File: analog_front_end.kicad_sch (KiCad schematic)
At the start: 14 parts, among them J3 Conn_01x03_Pin, J4 Conn_01x03_Pin, Q3 BC847,215, Q4 BSS316N, U7 OPA388IDBV

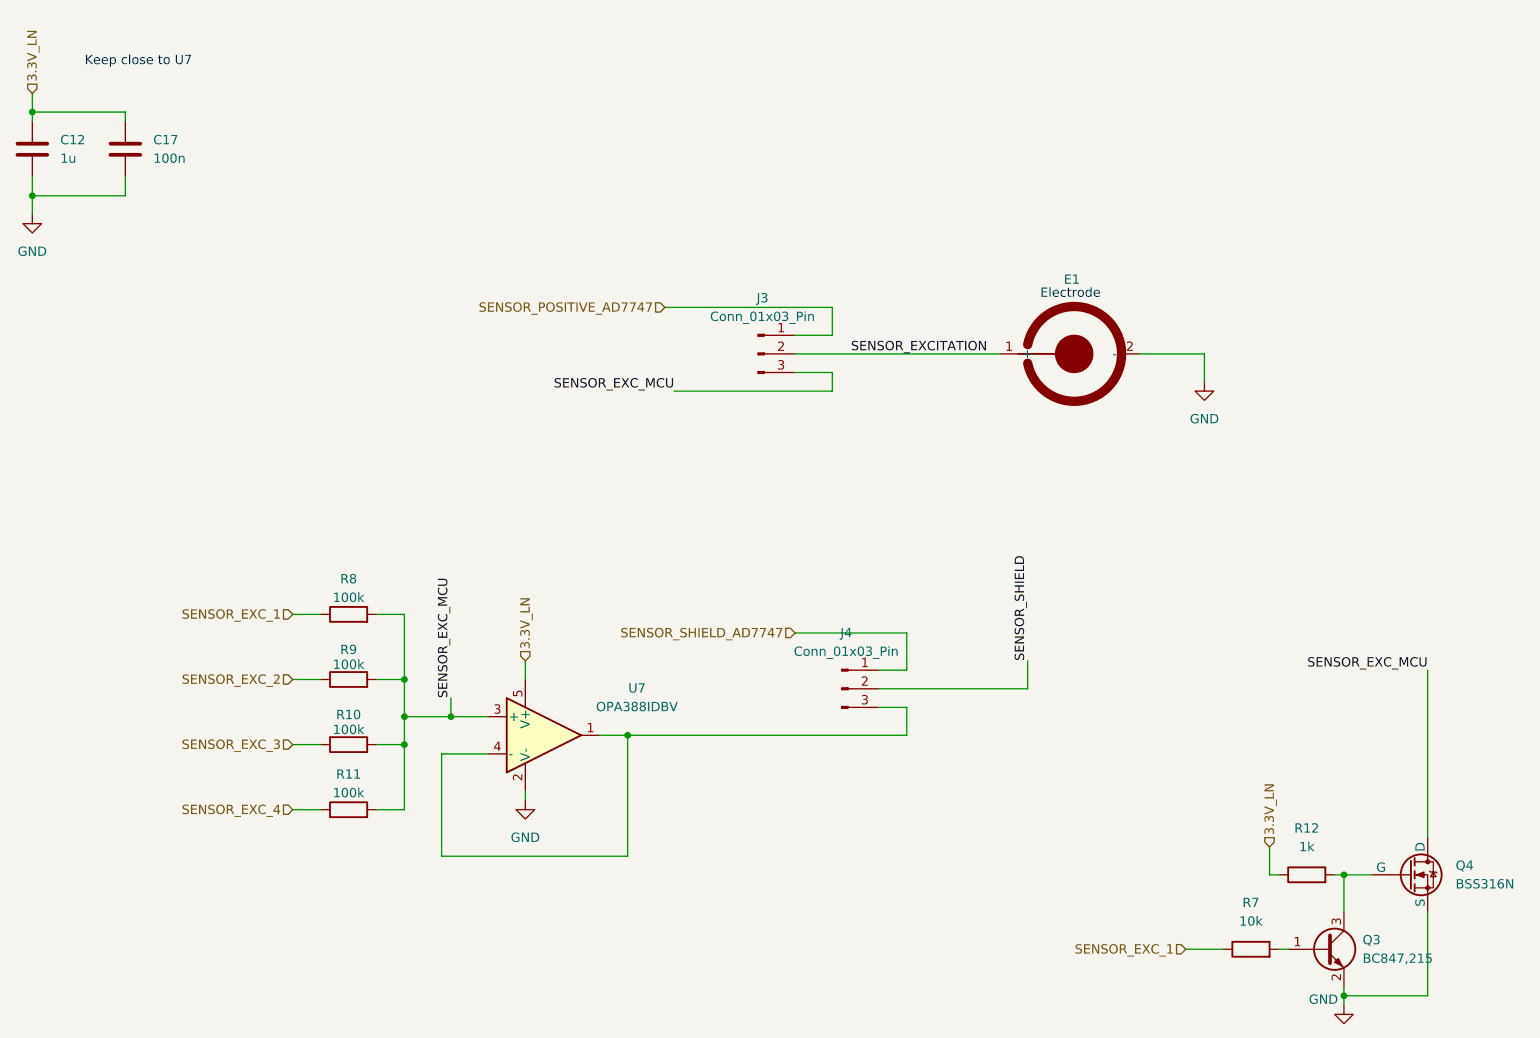
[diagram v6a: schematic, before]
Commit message: design: Assign LSCS and MPN reference to components
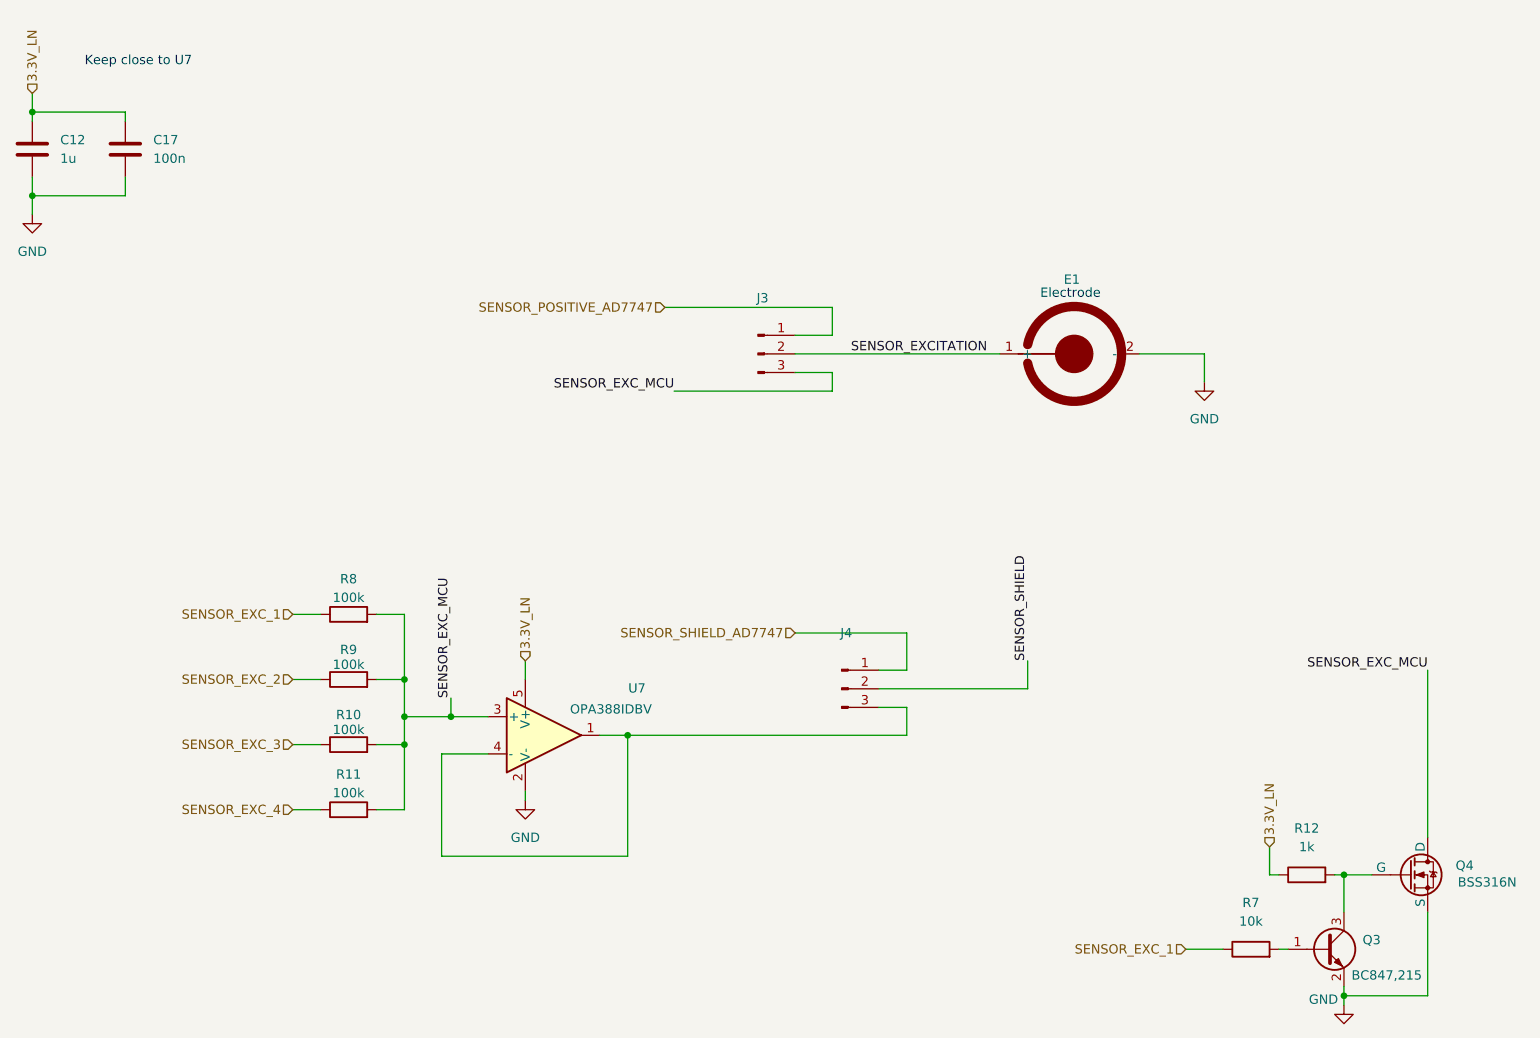
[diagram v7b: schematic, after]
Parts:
- C12: LCSC (none) -> C59782
- C17: LCSC (none) -> C14663
- E1: now left out of the parts list
- J3, J4: value Conn_01x03_Pin -> ~; LCSC (none) -> C5383112
- Q3: value BC847,215 -> ~; LCSC (none) -> C130417; MPN (none) -> BC847,215
- Q4: value BSS316N -> ~; LCSC (none) -> C19829413; MPN (none) -> BSS316N
- R10, R11, R8, R9: LCSC (none) -> C14675
- R12: LCSC (none) -> C22548
- R7: LCSC (none) -> C98220
- U7: value OPA388IDBV -> ~; LCSC (none) -> C1850240; MPN (none) -> OPA388IDBV
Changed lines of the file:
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@@
 		(on_board yes)
 		(dnp no)
-		(fields_autoplaced yes)
 		(property "Reference" "U7"
 			(at 99.06 105.3398 0)
@@
 			)
 		)
-		(property "Value" "OPA388IDBV"
+		(property "Value" "~"
 			(at 99.06 107.8798 0)
 			(effects
@@
 		)
 		(property "Description" "Operational amplifier, single"
+			(at 86.36 111.76 0)
+			(effects
+				(font
+					(size 1.27 1.27)
+				)
+				(hide yes)
+			)
+		)
+		(property "MPN" "OPA388IDBV"
+			(at 95.504 108.204 0)
+			(effects
+				(font
+					(size 1.27 1.27)
+				)
+			)
+		)
+		(property "LCSC" "C1850240"
 			(at 86.36 111.76 0)
 			(effects
@@
 			)
 		)
+		(property "LCSC" "C98220"
+			(at 182.88 140.97 0)
+			(effects
+				(font
+					(size 1.27 1.27)
+				)
+				(hide yes)
+			)
+		)
 		(pin "2"
 		)
@@
 			)
 		)
+		(property "LCSC" "C14675"
+			(at 59.69 113.03 0)
+			(effects
+				(font
+					(size 1.27 1.27)
+				)
+				(hide yes)
+			)
+		)
 		(pin "2"
 		)
@@
 		)
 		(property "Description" "Resistor"
+			(at 59.69 104.14 0)
+			(effects
+				(font
+					(size 1.27 1.27)
+				)
+				(hide yes)
+			)
+		)
+		(property "LCSC" "C14675"
 			(at 59.69 104.14 0)
 			(effects
@@
 			)
 		)
+		(property "LCSC" "C22548"
+			(at 190.5 130.81 0)
+			(effects
+				(font
+					(size 1.27 1.27)
+				)
+				(hide yes)
+			)
+		)
 		(pin "2"
 		)
@@
 		(on_board yes)
 		(dnp no)
-		(fields_autoplaced yes)
 		(property "Reference" "Q4"
 			(at 210.82 129.5399 0)
@@
 			)
 		)
-		(property "Value" "BSS316N"
+		(property "Value" "~"
 			(at 210.82 132.0799 0)
 			(effects
@@
 			)
 		)
-		(property "LCSC" ""
+		(property "LCSC" "C19829413"
 			(at 204.47 130.81 0)
 			(effects
@@
 				)
 				(hide yes)
+			)
+		)
+		(property "MPN" "BSS316N"
+			(at 215.138 131.826 0)
+			(effects
+				(font
+					(size 1.27 1.27)
+				)
 			)
 		)
@@
 			)
 		)
-		(property "Value" "Conn_01x03_Pin"
+		(property "Value" "~"
 			(at 116.205 54.61 0)
 			(effects
@@
 			)
 		)
+		(property "LCSC" "C5383112"
+			(at 115.57 59.69 0)
+			(effects
+				(font
+					(size 1.27 1.27)
+				)
+				(hide yes)
+			)
+		)
+		(property "MPN" ""
+			(at 115.57 59.69 0)
+			(effects
+				(font
+					(size 1.27 1.27)
+				)
+			)
+		)
 		(pin "3"
 		)
@@
 		(on_board yes)
 		(dnp no)
-		(fields_autoplaced yes)
 		(property "Reference" "Q3"
 			(at 198.12 139.6999 0)
@@
 			)
 		)
-		(property "Value" "BC847,215"
+		(property "Value" "~"
 			(at 198.12 142.2399 0)
 			(effects
@@
 			)
 		)
-		(property "LCSC" ""
+		(property "LCSC" "C130417"
 			(at 193.04 140.97 0)
 			(effects
@@
 				)
 				(hide yes)
+			)
+		)
+		(property "MPN" "BC847,215"
+			(at 201.422 144.526 0)
+			(effects
+				(font
+					(size 1.27 1.27)
+				)
 			)
 		)
@@
 			)
 		)
-		(property "Value" "Conn_01x03_Pin"
+		(property "Value" "~"
 			(at 127.635 100.33 0)
 			(effects
@@
 			)
 		)
+		(property "LCSC" "C5383112"
+			(at 127 105.41 0)
+			(effects
+				(font
+					(size 1.27 1.27)
+				)
+				(hide yes)
+			)
+		)
+		(property "MPN" ""
+			(at 127 105.41 0)
+			(effects
+				(font
+					(size 1.27 1.27)
+				)
+			)
+		)
 		(pin "3"
 		)
@@
 			)
 		)
+		(property "LCSC" "C14675"
+			(at 59.69 95.25 0)
+			(effects
+				(font
+					(size 1.27 1.27)
+				)
+				(hide yes)
+			)
+		)
 		(pin "2"
 		)
@@
 		)
 		(property "Description" "Resistor"
+			(at 59.69 121.92 0)
+			(effects
+				(font
+					(size 1.27 1.27)
+				)
+				(hide yes)
+			)
+		)
+		(property "LCSC" "C14675"
 			(at 59.69 121.92 0)
 			(effects
@@
 			)
 		)
+		(property "LCSC" "C14663"
+			(at 29.21 31.75 0)
+			(effects
+				(font
+					(size 1.27 1.27)
+				)
+				(hide yes)
+			)
+		)
 		(pin "1"
 		)
@@
 			)
 		)
-		(property "Description" "6.3V"
+		(property "Description" "10V"
+			(at 16.51 31.75 0)
+			(effects
+				(font
+					(size 1.27 1.27)
+				)
+				(hide yes)
+			)
+		)
+		(property "LCSC" "C59782"
 			(at 16.51 31.75 0)
 			(effects
@@
 		(unit 1)
 		(exclude_from_sim no)
-		(in_bom yes)
+		(in_bom no)
 		(on_board yes)
 		(dnp no)
@@
 			(at 158.75 59.69 0)
 			(effects
+				(font
+					(size 1.27 1.27)
+				)
+				(hide yes)
+			)
+		)
+		(property "LCSC" ""
+			(at 158.75 59.69 0)
+			(effects

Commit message: design: Assign the project version and project company from project variable, which are then substituted during the ci
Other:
- company: (none) -> ${COMPANY}
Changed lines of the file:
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@@
 	(title_block
 		(title "${SHEETNAME}")
+		(rev "${VERSION}")
+		(company "${COMPANY}")
 	)
 	(text "Keep close to U7\n\n\n\n"
